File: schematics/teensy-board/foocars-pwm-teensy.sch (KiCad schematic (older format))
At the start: 7 parts, among them J1 TOPTOP-14-LEFT, J2 BOTTOMBOTTOM-14-LEFT, J3 PWM_Input, J4 PWM_Output, J5 BattMon

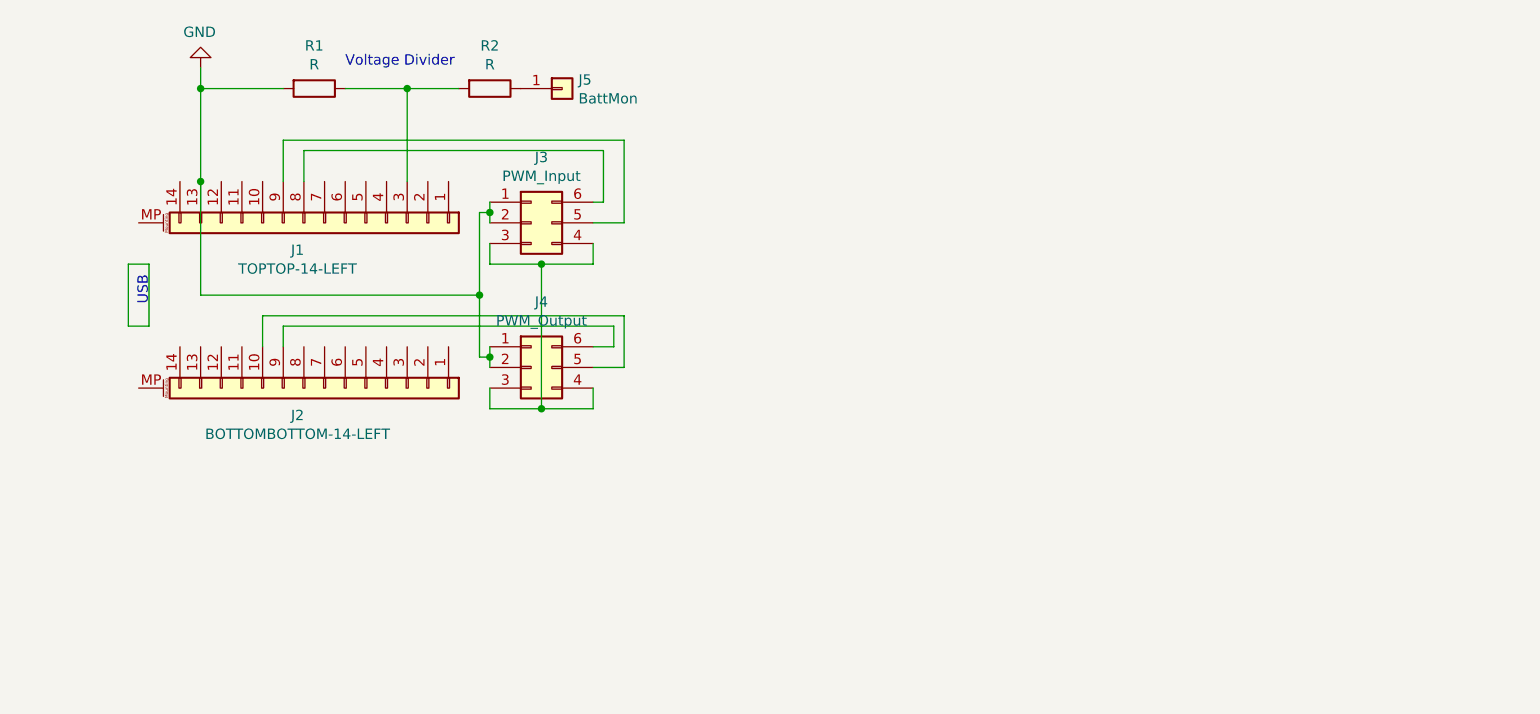
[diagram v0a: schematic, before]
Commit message: Updated PWM hat to have new inputs.
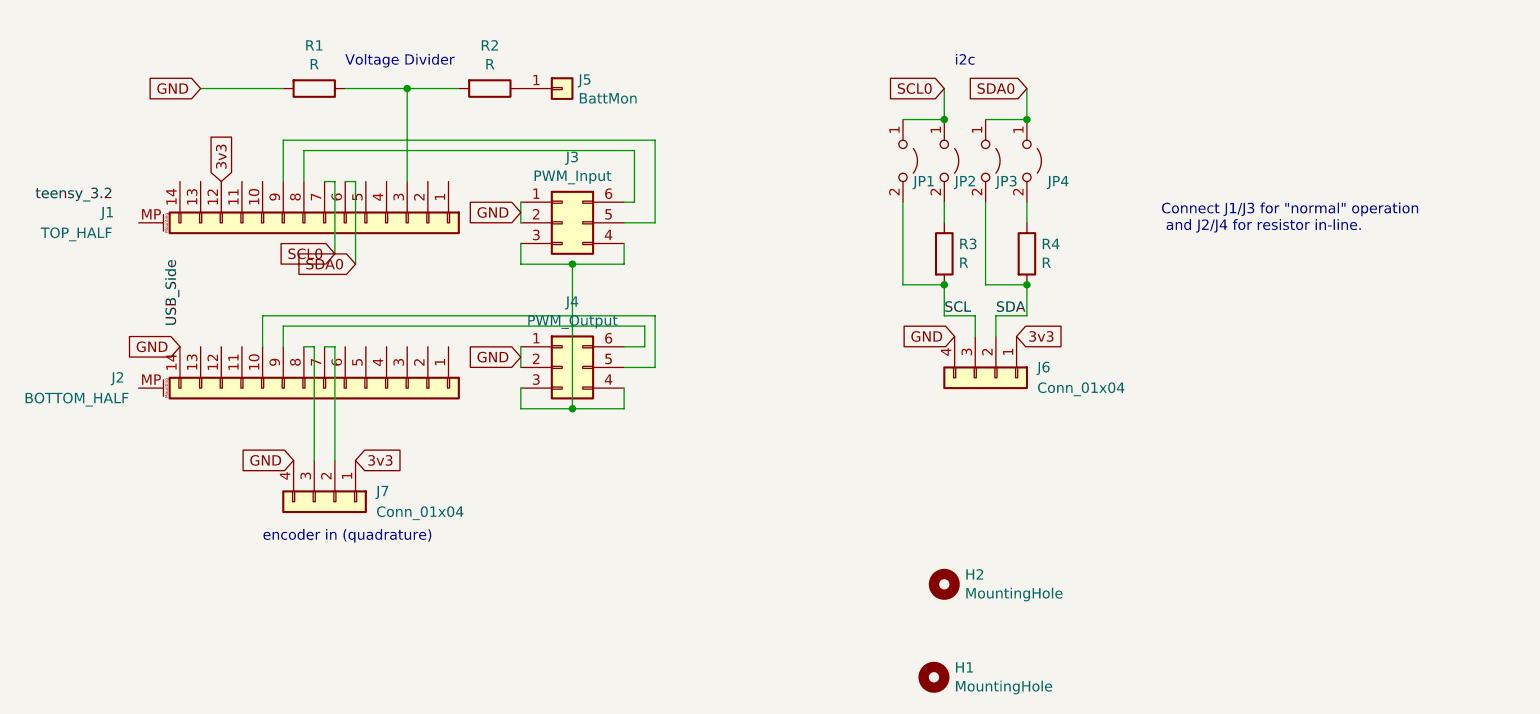
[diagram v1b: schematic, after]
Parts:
- added H1, H2: MountingHole, MountingHole:MountingHole_2.5mm_Pad, symbol Mechanical:MountingHole
- added J6, J7: Conn_01x04, Connector_PinHeader_2.54mm:PinHeader_1x04_P2.54mm_Horizontal, symbol Connector_Generic:Conn_01x04
- added JP1, JP2, JP3, JP4: Jumper_2_Open, Jumper:SolderJumper-2_P1.3mm_Open_TrianglePad1.0x1.5mm, symbol Jumper:Jumper_2_Open
- added R3, R4: R, Resistor_THT:R_Axial_DIN0204_L3.6mm_D1.6mm_P5.08mm_Horizontal, symbol Device:R
- J1: value TOPTOP-14-LEFT -> TOP_HALF
- J2: value BOTTOMBOTTOM-14-LEFT -> BOTTOM_HALF
- J5: footprint (none) -> Connector_PinHeader_2.54mm:PinHeader_1x01_P2.54mm_Vertical
- R1, R2: footprint (none) -> Resistor_THT:R_Axial_DIN0204_L3.6mm_D1.6mm_P5.08mm_Horizontal
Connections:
- net GND: now also J2.14 (Pin_14), J6.4 (Pin_4), J7.4 (Pin_4); no longer J1.13 (Pin_13)
- net 3v3: now reaches J1.12 (Pin_12)
- net 3v3: now also J6.1 (Pin_1), J7.1 (Pin_1)
- net SDA0: now reaches J1.6 (Pin_6)
- net SDA0: now also JP3.1 (A), JP4.1 (A)
- net SCL0: now reaches J1.7 (Pin_7)
- net SCL0: now also JP1.1 (A), JP2.1 (A)
- net at J2.7 (Pin_7): now also J7.2 (Pin_2)
- net at J2.8 (Pin_8): now also J7.3 (Pin_3)
- new net: JP2.2 (B), R3.1
- new net: JP4.2 (B), R4.1
- new net SCL: J6.3 (Pin_3), JP1.2 (B), R3.2
- new net SDA: J6.2 (Pin_2), JP3.2 (B), R4.2
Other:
- note added: "Connect J1/J3 for "normal" operation\n and J2/J4 for resistor in-line."
- note added: "encoder in (quadrature)\n"
- note added: "i2c\n"
- note removed: "USB\n"
- moved on the sheet: J3, J4

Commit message: Added new layout, new pins, added TVS diode.
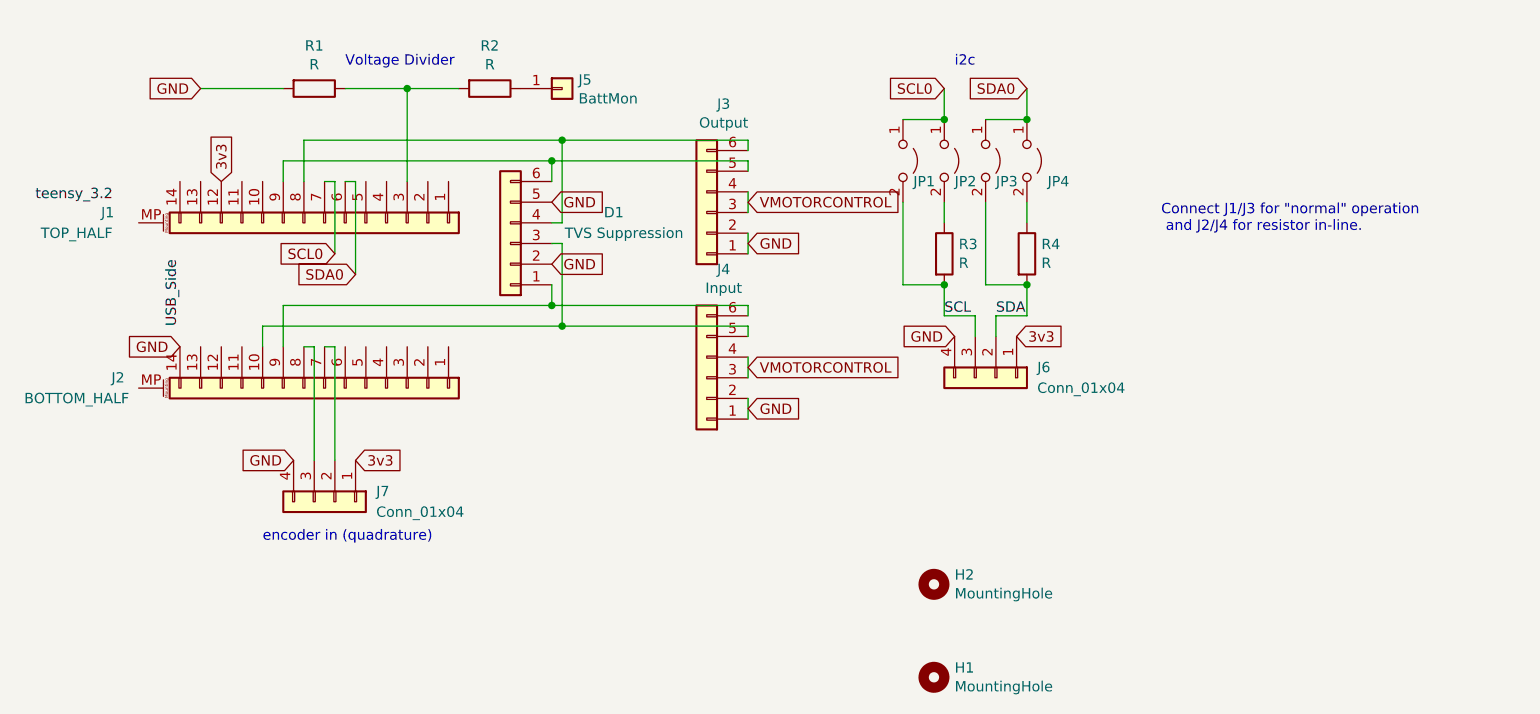
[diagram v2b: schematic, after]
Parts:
- removed J3: PWM_Input, Connector_PinSocket_2.54mm:PinSocket_2x03_P2.54mm_Horizontal, symbol Connector_Generic:Conn_02x03_Counter_Clockwise
- removed J4: PWM_Output, Connector_PinHeader_2.54mm:PinHeader_2x03_P2.54mm_Horizontal, symbol Connector_Generic:Conn_02x03_Counter_Clockwise
- added D1: TVS Suppression, Package_TO_SOT_SMD:SOT-23-6_Handsoldering, symbol Connector_Generic:Conn_01x06
- added J3: Output, Connector_PinHeader_2.54mm:PinHeader_2x03_P2.54mm_Horizontal, symbol Connector_Generic:Conn_01x06
- added J4: Input, Connector_PinHeader_2.54mm:PinHeader_2x03_P2.54mm_Horizontal, symbol Connector_Generic:Conn_01x06
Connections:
- net GND: now also D1.2 (Pin_2), D1.5 (Pin_5), J3.1 (Pin_1), J3.2 (Pin_2), J4.1 (Pin_1), J4.2 (Pin_2)
- net at J1.8 (Pin_8): now also D1.4 (Pin_4), J3.6 (Pin_6)
- net at J1.9 (Pin_9): now also D1.6 (Pin_6), J3.5 (Pin_5)
- net at J2.10 (Pin_10): now also D1.3 (Pin_3), J4.5 (Pin_5)
- net at J2.9 (Pin_9): now also D1.1 (Pin_1), J4.6 (Pin_6)
- new net VMOTORCONTROL: J3.3 (Pin_3), J3.4 (Pin_4), J4.3 (Pin_3), J4.4 (Pin_4)
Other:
- moved on the sheet: H2
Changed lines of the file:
@@
 encoding utf-8
 Sheet 1 1
-Title ""
-Date ""
-Rev ""
-Comp ""
+Title "Foocars Microcontroller Hat"
+Date "2020-08-21"
+Rev "1"
+Comp "Rutgers University Games Research & Immersive Design + Rutgers Makerspace"
 Comment1 ""
 Comment2 ""
@@
 $EndComp
 $Comp
-L Connector_Generic:Conn_02x03_Counter_Clockwise J4
-U 1 1 5D13893A
-P 6400 2700
-F 0 "J4" H 6450 3017 50  0000 C CNN
-F 1 "PWM_Output" H 6450 2926 50  0000 C CNN
-F 2 "Connector_PinHeader_2.54mm:PinHeader_2x03_P2.54mm_Horizontal" H 6400 2700 50  0001 C CNN
-F 3 "~" H 6400 2700 50  0001 C CNN
-	1    6400 2700
-	1    0    0    -1
-$EndComp
-$Comp
-L Connector_Generic:Conn_02x03_Counter_Clockwise J3
-U 1 1 5D13BA5A
-P 6400 2000
-F 0 "J3" H 6450 2317 50  0000 C CNN
-F 1 "PWM_Input" H 6450 2226 50  0000 C CNN
-F 2 "Connector_PinSocket_2.54mm:PinSocket_2x03_P2.54mm_Horizontal" H 6400 2000 50  0001 C CNN
-F 3 "~" H 6400 2000 50  0001 C CNN
-	1    6400 2000
-	1    0    0    -1
-$EndComp
-$Comp
 L Connector_Generic_MountingPin:Conn_01x14_MountingPin J1
 U 1 1 5D123A95
@@
 	0    1    1    0
 $EndComp
-Wire Wire Line
-	5050 2600 5050 2500
-Wire Wire Line
-	6200 2100 6200 2200
-Wire Wire Line
-	6200 2200 6450 2200
-Wire Wire Line
-	6700 2200 6700 2100
-Wire Wire Line
-	6200 2800 6200 2900
-Wire Wire Line
-	6200 2900 6450 2900
-Wire Wire Line
-	6700 2900 6700 2800
-Wire Wire Line
-	6700 2000 6850 2000
-Wire Wire Line
-	6850 2000 6850 1600
-Wire Wire Line
-	5050 1600 5050 1800
-Wire Wire Line
-	6750 1650 6750 1900
-Wire Wire Line
-	6750 1900 6700 1900
-Wire Wire Line
-	5150 1650 5150 1800
-Wire Wire Line
-	6700 2600 6800 2600
-Wire Wire Line
-	6800 2600 6800 2500
-Wire Wire Line
-	6850 2450 6850 2700
-Wire Wire Line
-	6850 2700 6700 2700
-Wire Wire Line
-	4950 2450 4950 2600
-Wire Wire Line
-	6450 2200 6450 2900
-Connection ~ 6450 2200
-Wire Wire Line
-	6450 2200 6700 2200
-Connection ~ 6450 2900
-Wire Wire Line
-	6450 2900 6700 2900
 $Comp
 L Connector_Generic:Conn_01x01 J5
@@
 Text GLabel 4550 2600 0    50   Input ~ 0
 GND
-Text GLabel 6200 1950 0    50   Input ~ 0
-GND
 Text GLabel 4650 1350 0    50   Input ~ 0
 GND
@@
 Wire Wire Line
 	5350 1800 5400 1800
-Wire Wire Line
-	6200 2600 6200 2700
-Wire Wire Line
-	6200 1900 6200 2000
-Text GLabel 6200 2650 0    50   Input ~ 0
-GND
-Wire Wire Line
-	5050 1600 6850 1600
-Wire Wire Line
-	5150 1650 6750 1650
-Wire Wire Line
-	4950 2450 6850 2450
-Wire Wire Line
-	5050 2500 6800 2500
 Text GLabel 5300 2150 0    50   Input ~ 0
 SCL0
-Text GLabel 5400 2200 0    50   Input ~ 0
+Text GLabel 5400 2250 0    50   Input ~ 0
 SDA0
-Wire Wire Line
-	5400 1800 5400 2200
 Text GLabel 8250 1350 0    50   Input ~ 0
 SCL0
@@
 L Mechanical:MountingHole H2
 U 1 1 5F4B0E4F
-P 8250 3750
-F 0 "H2" H 8350 3796 50  0000 L CNN
-F 1 "MountingHole" H 8350 3705 50  0000 L CNN
-F 2 "MountingHole:MountingHole_2.5mm_Pad" H 8250 3750 50  0001 C CNN
-F 3 "~" H 8250 3750 50  0001 C CNN
-	1    8250 3750
+P 8200 3750
+F 0 "H2" H 8300 3796 50  0000 L CNN
+F 1 "MountingHole" H 8300 3705 50  0000 L CNN
+F 2 "MountingHole:MountingHole_2.5mm_Pad" H 8200 3750 50  0001 C CNN
+F 3 "~" H 8200 3750 50  0001 C CNN
+	1    8200 3750
 	1    0    0    -1
 $EndComp
@@
 	1    0    0    -1
 $EndComp
+$Comp
+L Connector_Generic:Conn_01x06 J4
+U 1 1 5F470182
+P 7100 2750
+F 0 "J4" H 7018 2225 50  0000 C CNN
+F 1 "Input" H 7018 2316 50  0000 C CNN
+F 2 "Connector_PinHeader_2.54mm:PinHeader_2x03_P2.54mm_Horizontal" H 7100 2750 50  0001 C CNN
+F 3 "~" H 7100 2750 50  0001 C CNN
+	1    7100 2750
+	-1   0    0    1
+$EndComp
+Wire Wire Line
+	7300 2950 7300 2850
+Text GLabel 7300 2900 2    50   Input ~ 0
+GND
+Wire Wire Line
+	7300 2750 7300 2650
+Text GLabel 7300 2700 2    50   Input ~ 0
+VMOTORCONTROL
+$Comp
+L Connector_Generic:Conn_01x06 J3
+U 1 1 5F483E45
+P 7100 1950
+F 0 "J3" H 7018 1425 50  0000 C CNN
+F 1 "Output" H 7018 1516 50  0000 C CNN
+F 2 "Connector_PinHeader_2.54mm:PinHeader_2x03_P2.54mm_Horizontal" H 7100 1950 50  0001 C CNN
+F 3 "~" H 7100 1950 50  0001 C CNN
+	1    7100 1950
+	-1   0    0    1
+$EndComp
+Wire Wire Line
+	7300 2150 7300 2050
+Text GLabel 7300 2100 2    50   Input ~ 0
+GND
+Wire Wire Line
+	7300 1950 7300 1850
+Text GLabel 7300 1900 2    50   Input ~ 0
+VMOTORCONTROL
+Wire Wire Line
+	7300 2400 7300 2450
+Wire Wire Line
+	5050 2400 5050 2600
+Wire Wire Line
+	7300 2550 7300 2500
+Wire Wire Line
+	4950 2500 4950 2600
+Wire Wire Line
+	7300 1750 7300 1700
+Wire Wire Line
+	5050 1800 5050 1700
+Wire Wire Line
+	5150 1600 5150 1800
+Wire Wire Line
+	7300 1600 7300 1650
+Wire Wire Line
+	5400 1800 5400 2250
+$Comp
+L Connector_Generic:Conn_01x06 D1
+U 1 1 5F4C91A1
+P 6150 2100
+F 0 "D1" H 5650 1950 50  0000 C CNN
+F 1 "TVS Suppression" H 5600 2050 50  0000 C CNN
+F 2 "Package_TO_SOT_SMD:SOT-23-6_Handsoldering" H 6150 2100 50  0001 C CNN
+F 3 "https://www.digikey.com/product-detail/en/comchip-technology/CPDT6-5V4-HF/641-1086-1-ND/1121208" H 6150 2100 50  0001 C CNN
+	1    6150 2100
+	-1   0    0    1
+$EndComp
+Wire Wire Line
+	5050 2400 6350 2400
+Wire Wire Line
+	4950 2500 6400 2500
+Wire Wire Line
+	5050 1700 6350 1700
+Text GLabel 6350 2200 2    50   Input ~ 0
+GND
+Text GLabel 6350 1900 2    50   Input ~ 0
+GND
+Wire Wire Line
+	6350 1800 6350 1700
+Connection ~ 6350 1700
+Wire Wire Line
+	6350 1700 7300 1700
+Wire Wire Line
+	5150 1600 6400 1600
+Wire Wire Line
+	6400 1600 6400 2000
+Wire Wire Line
+	6400 2000 6350 2000
+Connection ~ 6400 1600
+Wire Wire Line
+	6400 1600 7300 1600
+Wire Wire Line
+	6350 2100 6400 2100
+Wire Wire Line
+	6400 2100 6400 2500
+Connection ~ 6400 2500
+Wire Wire Line
+	6400 2500 7300 2500
+Wire Wire Line
+	6350 2300 6350 2400
+Connection ~ 6350 2400
+Wire Wire Line
+	6350 2400 7300 2400
 $EndSCHEMATC

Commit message: Swap ground pins, review with Rick.
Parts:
- J5: footprint Connector_PinHeader_2.54mm:PinHeader_1x01_P2.54mm_Vertical -> Connector_PinHeader_2.54mm:PinHeader_1x02_P2.54mm_Vertical; symbol Connector_Generic:Conn_01x01 -> Connector_Generic:Conn_01x02
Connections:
- net 3v3: now also J6.4 (Pin_4), J7.4 (Pin_4); no longer J6.1 (Pin_1), J7.1 (Pin_1)
- net GND: now also J6.1 (Pin_1), J7.1 (Pin_1); no longer J6.4 (Pin_4), J7.4 (Pin_4), R1.2
- net at J1.13 (Pin_13): now also J5.1 (Pin_1), R1.2
- net at R2.1: now also J5.2 (Pin_2); no longer J5.1 (Pin_1)
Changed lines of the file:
@@
 $EndComp
 $Comp
-L Connector_Generic:Conn_01x01 J5
+L Connector_Generic:Conn_01x02 J5
 U 1 1 5D24D8A7
-P 6400 1350
-F 0 "J5" H 6479 1392 50  0000 L CNN
-F 1 "BattMon" H 6479 1301 50  0000 L CNN
-F 2 "Connector_PinHeader_2.54mm:PinHeader_1x01_P2.54mm_Vertical" H 6400 1350 50  0001 C CNN
-F 3 "~" H 6400 1350 50  0001 C CNN
-	1    6400 1350
+P 6400 1250
+F 0 "J5" H 6479 1292 50  0000 L CNN
+F 1 "BattMon" H 6479 1201 50  0000 L CNN
+F 2 "Connector_PinHeader_2.54mm:PinHeader_1x02_P2.54mm_Vertical" H 6400 1250 50  0001 C CNN
+F 3 "~" H 6400 1250 50  0001 C CNN
+	1    6400 1250
 	1    0    0    -1
 $EndComp
@@
 $EndComp
 Wire Wire Line
-	5050 1350 4650 1350
-Wire Wire Line
 	5350 1350 5650 1350
 Wire Wire Line
@@
 USB_Side
 Text GLabel 4550 2600 0    50   Input ~ 0
-GND
-Text GLabel 4650 1350 0    50   Input ~ 0
 GND
 Wire Wire Line
@@
 Text GLabel 4750 1800 1    50   Input ~ 0
 3v3
+Text GLabel 8300 2550 0    50   Input ~ 0
+3v3
 Text GLabel 8600 2550 2    50   Input ~ 0
-3v3
-Text GLabel 8300 2550 0    50   Input ~ 0
 GND
 Text Label 8250 2450 0    50   ~ 0
@@
 	0    1    1    0
 $EndComp
+Text GLabel 5400 3150 2    50   Input ~ 0
+GND
 Text GLabel 5100 3150 0    50   Input ~ 0
-GND
-Text GLabel 5400 3150 2    50   Input ~ 0
 3v3
 Text Notes 4950 3550 0    50   ~ 0
@@
 Wire Wire Line
 	6350 2400 7300 2400
+Wire Wire Line
+	4650 1350 4900 1350
+Wire Wire Line
+	4650 1350 4650 1800
+Wire Wire Line
+	4900 1350 4900 1000
+Wire Wire Line
+	4900 1000 6200 1000
+Wire Wire Line
+	6200 1000 6200 1250
+Connection ~ 4900 1350
+Wire Wire Line
+	4900 1350 5050 1350
 $EndSCHEMATC
